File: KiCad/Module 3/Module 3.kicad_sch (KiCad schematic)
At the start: 20 parts, among them SW1 BLUE_LED, SW2 YELLOW_LED, SW3 GREEN_LED, SW4 RED_LED, SW5 SW_Lock_NC_NO

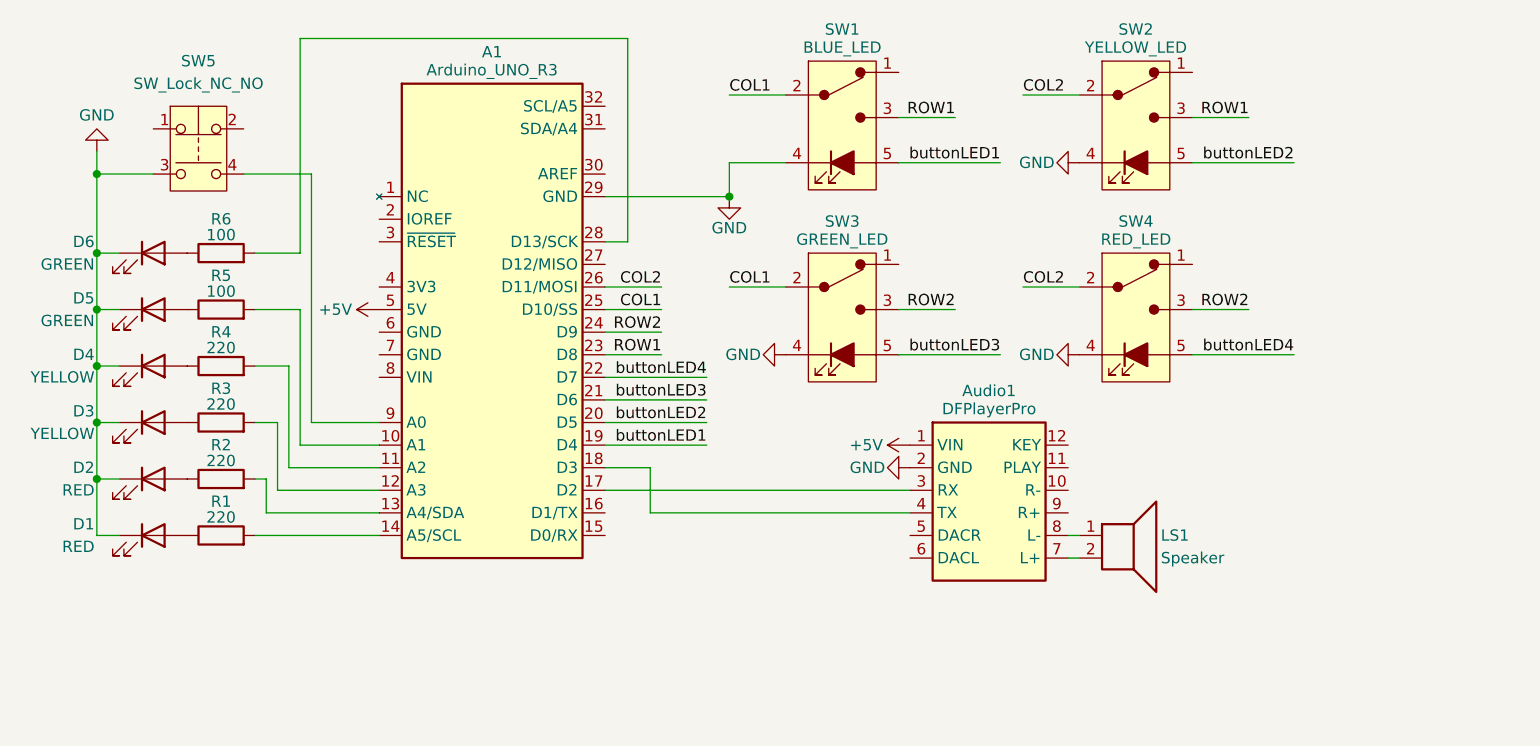
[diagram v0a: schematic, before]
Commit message: Replaced Arduino with ESP32 in Module 3 schematic
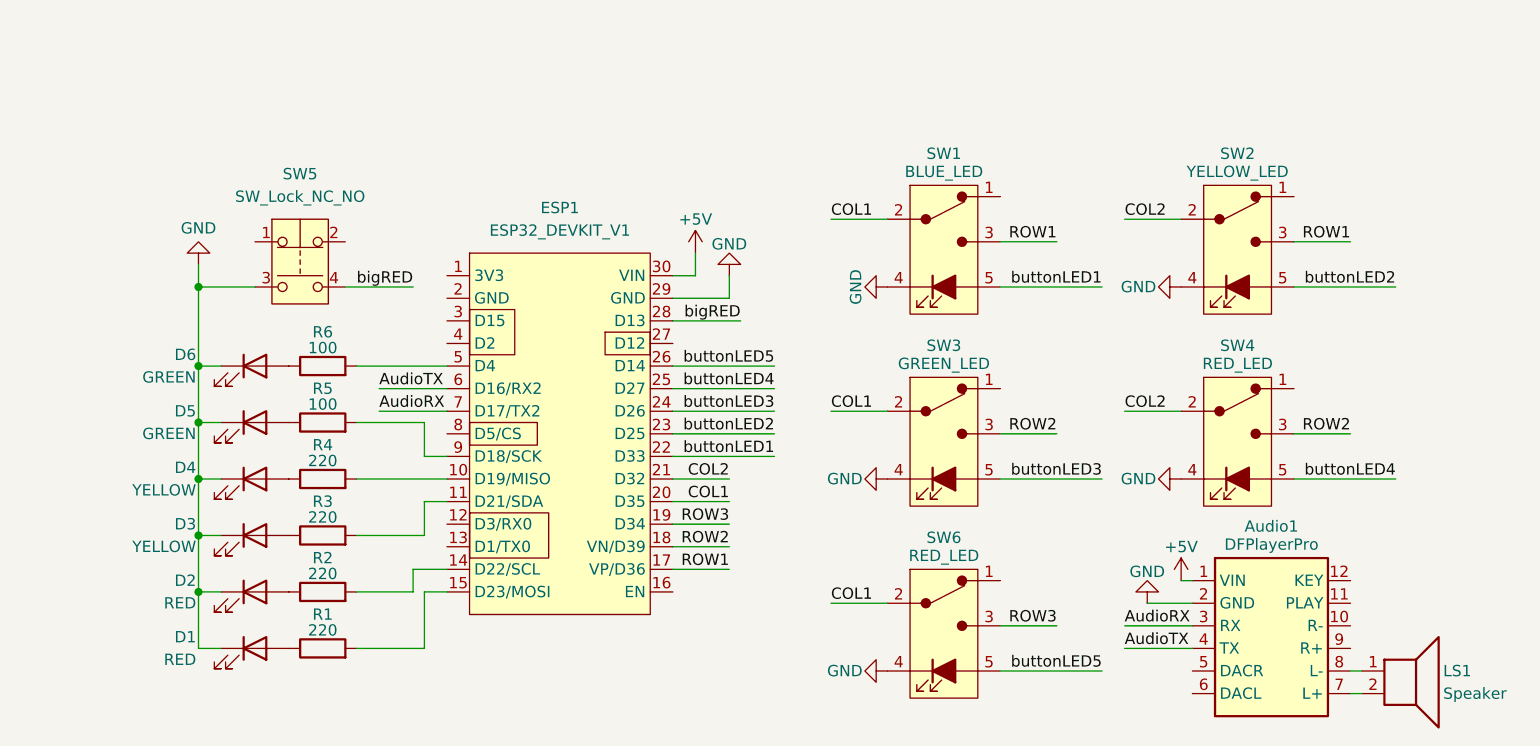
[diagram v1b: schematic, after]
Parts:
- removed A1: Arduino_UNO_R3, symbol IEEE_CS_Escape_Room_Symbols_v1:Arduino_UNO_R3
- added ESP1: ESP32_DEVKIT_V1, symbol IEEE_CS_Escape_Room_Symbols_v2:ESP32_DEVKIT_V1
- added SW6: RED_LED, symbol IEEE_CS_Escape_Room_Symbols_v1:SW_Push_SPDT_LED
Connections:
- net +5V: now also ESP1.30 (VIN)
- net COL1: now also ESP1.20 (D35), SW6.2 (C)
- net COL2: now also ESP1.21 (D32)
- net GND: now also ESP1.29 (GND), SW6.4 (K)
- net ROW1: now also ESP1.17 (VP/D36)
- net ROW2: now also ESP1.18 (VN/D39)
- net buttonLED1: now also ESP1.22 (D33)
- net buttonLED2: now also ESP1.23 (D25)
- net buttonLED3: now also ESP1.24 (D26)
- net buttonLED4: now also ESP1.25 (D27)
- net at R5.2: now also ESP1.9 (D18/SCK)
- net at R6.2: now also ESP1.5 (D4)
- net at R4.2: now also ESP1.10 (D19/MISO)
- net at R3.2: now also ESP1.11 (D21/SDA)
- net at R2.2: now also ESP1.14 (D22/SCL)
- net at R1.2: now also ESP1.15 (D23/MOSI)
- net AudioRX: now reaches Audio1.3 (RX)
- net AudioRX: now also ESP1.7 (D17/TX2)
- net AudioTX: now reaches Audio1.4 (TX)
- net AudioTX: now also ESP1.6 (D16/RX2)
- net bigRED: now reaches SW5.4
- net bigRED: now also ESP1.28 (D13)
- new net ROW3: ESP1.19 (D34), SW6.3 (NO)
- new net buttonLED5: ESP1.26 (D14), SW6.5 (A)
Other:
- moved on the sheet: Audio1, D1, D2, D3, D4, D5, D6, LS1, R1, R2, R3, R4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
